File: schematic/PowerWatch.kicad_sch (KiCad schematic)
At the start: 17 parts, among them K1 SANYOU_SRD_Form_C, Q1 PN2222A, U1 4N25

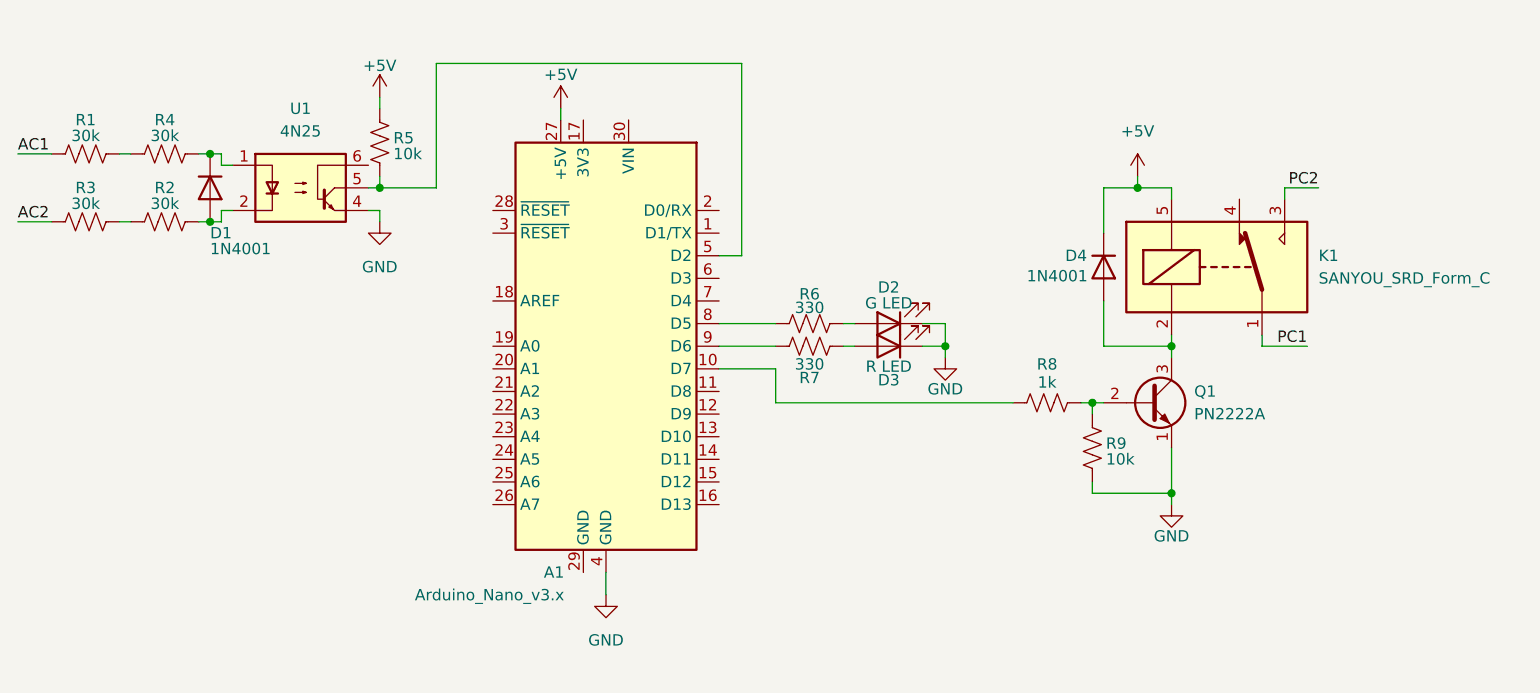
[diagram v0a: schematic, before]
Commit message: update input res values and output pins
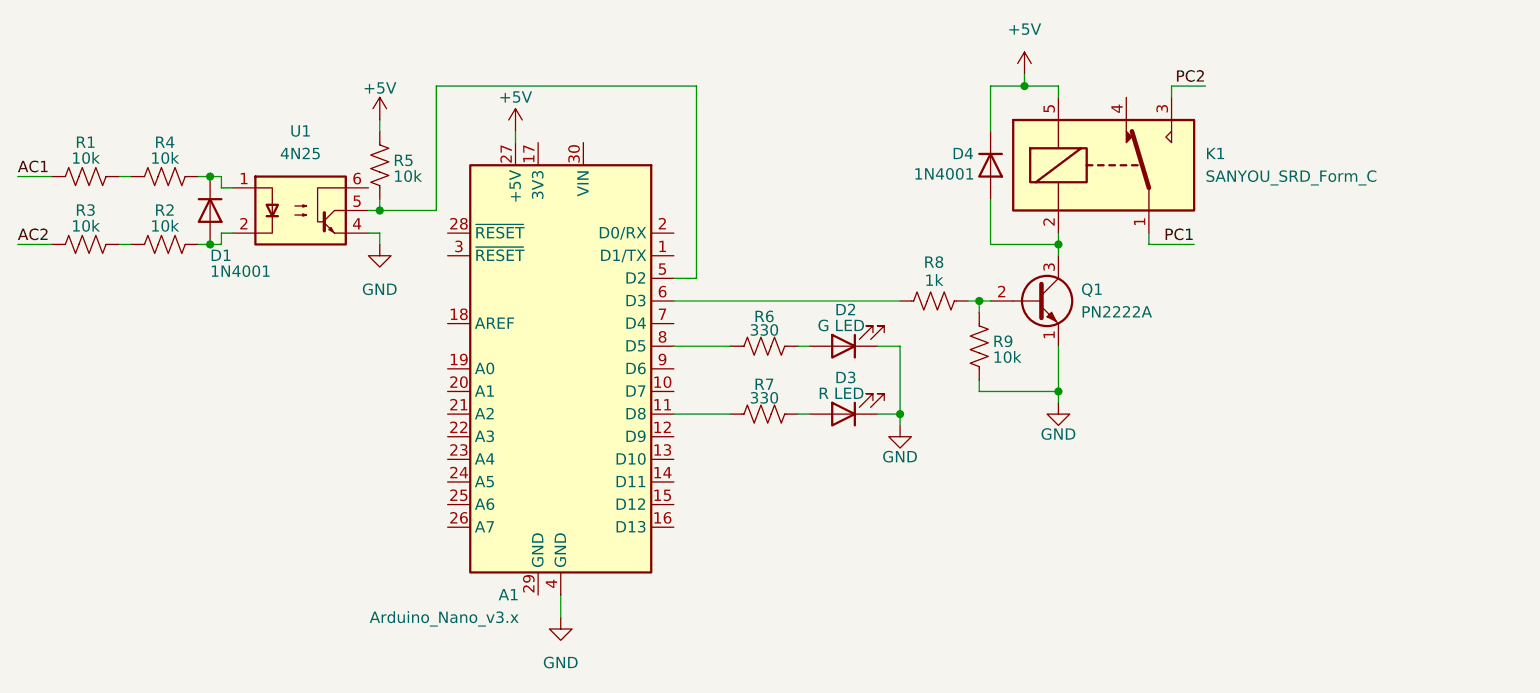
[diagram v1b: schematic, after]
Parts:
- R1, R2, R3, R4: value 30k -> 10k
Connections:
- net at R8.1: now also A1.6 (D3); no longer A1.10 (D7)
- net at A1.11 (D8): now also R7.1
- net at A1.9 (D6): no longer R7.1
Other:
- moved on the sheet: A1, D1, D2, D3, D4, K1, Q1, R1, R2, R3, R4, R5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
